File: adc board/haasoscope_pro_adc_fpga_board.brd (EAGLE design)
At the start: 224.5 x 160 mm, 635 parts, among them CN2 12Vin, IC1 ADC12DL2500ACF, IC10 TPS72325DBVR, IC13 LMH5401IRMST, IC14 LMH6401IRMZR, IC15 SN74AVC4T774PWR, IC17 DAC8562SDGSR, IC18 TLV9102IPWR, IC2 SN74AVC4T774PWR, IC21 LMH5401IRMST, IC22 TPS7A7200RGTR, IC23 TPS7A7200RGTR, IC24 TPS7A7200RGTR, IC25 TPS72325DBVR, IC26 TPS7A7200RGTR, IC27 TPS7A7200RGTR, IC28 TPS7A7200RGTR, IC29 LMH6401IRMZR, IC3 ADC122S021CIMM_NOPB, IC30 SN74AVC4T774PWR, IC33 TLV9102IPWR, IC4 TLV9102IPWR, IC5 EP4CE30F23C6N, IC6 EPCQ16ASI8N, IC7 TPS7A7200RGTR, IC8 FT232HQ, IC9 93LC56B, J1 2p-2.54, J11 8pin, J15 test1, J2 test1, J3 2p-2.54, J30 2p-2.54, J31 2p-2.54, J32 2p-2.54, J33 2p-2.54, J34 2p-2.54, J35 2p-2.54, J36 2p-2.54, J37 2p-2.54, J39 2p-2.54, J4 2p-2.54, J40 2p-2.54, J41 2p-2.54, J42 2p-2.54, J43 2p-2.54, J44 2p-2.54, J45 2p-2.54, J46 2p-2.54, J5 1x4, K1 G6K-2F-RF-T-TR03_DC5, K2 G6K-2F-RF-T-TR03_DC5, K3 G6K-2F-RF-T-TR03_DC5, K4 G6K-2F-RF-T-TR03_DC5, K5 G6K-2F-RF-T-TR03_DC5, K6 TLP3475_TP,F, K7 TLP3475_TP,F, Q1 S8050, Q2 FDN340P, Q4 S8050, Q5 S8050, Q7 S8050, Q8 S8050, Q9 S8050, SW3 SKQGADE010, SW4 SKQGADE010, U2 ADF4350BCPZ, X1 USBC, Y2 OSCILLATORSMD-5X3, Y3 12MHz

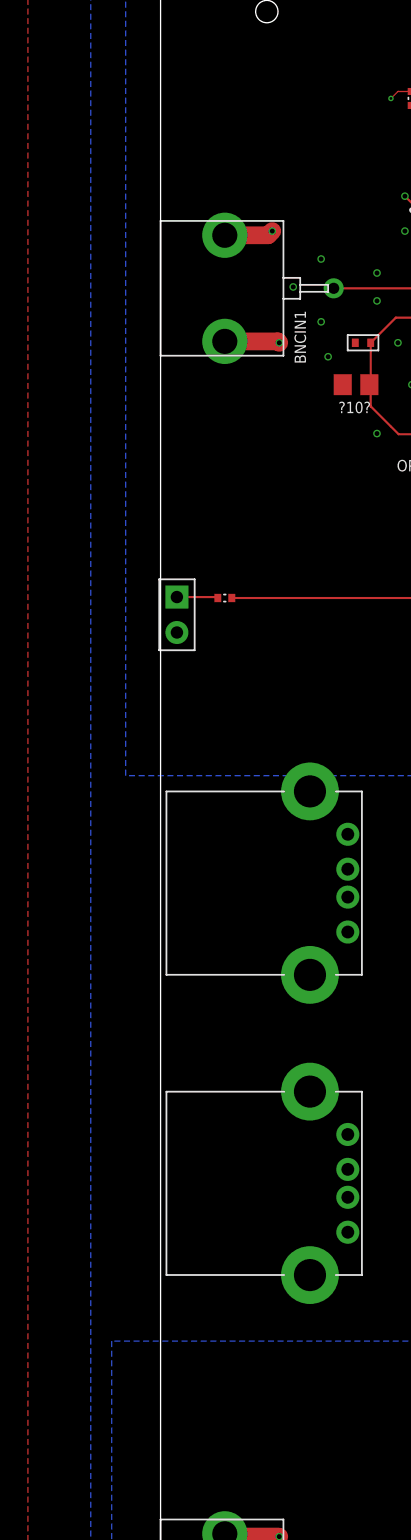
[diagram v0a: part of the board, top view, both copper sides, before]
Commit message: add light pipes for front leds
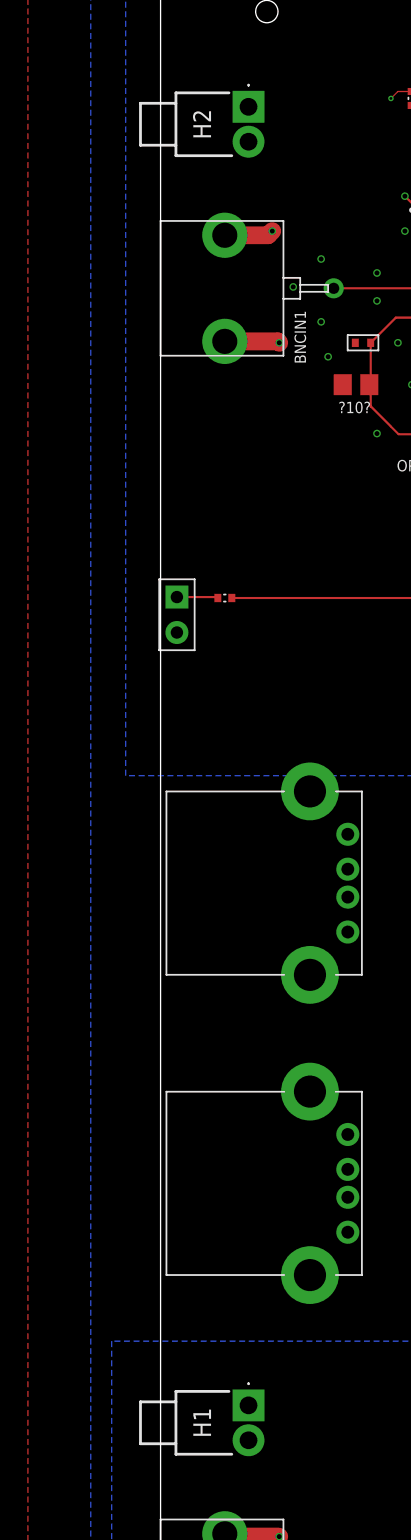
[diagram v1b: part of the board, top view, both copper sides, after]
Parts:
- added H1, H2: SLP3-150-100-F, SLP3-150-100-F:SLP3150100F
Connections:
- net GND: now also H1.1, H1.2, H2.1, H2.2
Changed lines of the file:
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@@
 <setting verticaltext="up"/>
 </settings>
-<grid distance="1" unitdist="mm" unit="mm" style="lines" multiple="1" display="no" altdistance="0.01" altunitdist="mm" altunit="mm"/>
+<grid distance="1" unitdist="mm" unit="mm" style="lines" multiple="1" display="yes" altdistance="0.01" altunitdist="mm" altunit="mm"/>
 <layers>
 <layer number="1" name="top" color="12" fill="1" visible="yes" active="yes"/>
@@
 <element name="R167" library="FlashPCB_Resistors" package="RES-0402" value="10k" x="203" y="94" smashed="yes"/>
 <element name="R246" library="FlashPCB_Resistors" package="RES-0402" value="10k" x="203.01" y="95.41" smashed="yes"/>
+<element name="H1" library="SLP3-150-100-F" package="SLP3150100F" value="SLP3-150-100-F" x="6.3" y="53.4" smashed="yes" rot="R270">
+<attribute name="DESCRIPTION" value="LED Light Pipes Light Pipe Rigid 3mm Right Angle" x="6.3" y="53.4" size="0.8128" layer="27" rot="R270" display="off"/>
+<attribute name="HEIGHT" value="5.4mm" x="6.3" y="53.4" size="0.8128" layer="27" rot="R270" display="off"/>
+<attribute name="MANUFACTURER_NAME" value="Bivar" x="6.3" y="53.4" size="0.8128" layer="27" rot="R270" display="off"/>
+<attribute name="MANUFACTURER_PART_NUMBER" value="SLP3-150-100-F" x="6.3" y="53.4" size="0.8128" layer="27" rot="R270" display="off"/>
+<attribute name="MOUSER_PART_NUMBER" value="749-SLP3-150-100-F" x="6.3" y="53.4" size="0.8128" layer="27" rot="R270" display="off"/>
+<attribute name="MOUSER_PRICE-STOCK" value="https://www.mouser.co.uk/ProductDetail/Bivar/SLP3-150-100-F?qs=6qR8IwHvvod8lAECqeEkXA%3D%3D" x="6.3" y="53.4" size="0.8128" layer="27" rot="R270" display="off"/>
+<attribute name="NAME" x="2.98" y="52.15" size="1.27" layer="25" rot="R270" align="center"/>
+</element>
+<element name="H2" library="SLP3-150-100-F" package="SLP3150100F" value="SLP3-150-100-F" x="6.3" y="146.4" smashed="yes" rot="R270">
+<attribute name="DESCRIPTION" value="LED Light Pipes Light Pipe Rigid 3mm Right Angle" x="6.3" y="146.4" size="0.8128" layer="27" rot="R270" display="off"/>
+<attribute name="HEIGHT" value="5.4mm" x="6.3" y="146.4" size="0.8128" layer="27" rot="R270" display="off"/>
+<attribute name="MANUFACTURER_NAME" value="Bivar" x="6.3" y="146.4" size="0.8128" layer="27" rot="R270" display="off"/>
+<attribute name="MANUFACTURER_PART_NUMBER" value="SLP3-150-100-F" x="6.3" y="146.4" size="0.8128" layer="27" rot="R270" display="off"/>
+<attribute name="MOUSER_PART_NUMBER" value="749-SLP3-150-100-F" x="6.3" y="146.4" size="0.8128" layer="27" rot="R270" display="off"/>
+<attribute name="MOUSER_PRICE-STOCK" value="https://www.mouser.co.uk/ProductDetail/Bivar/SLP3-150-100-F?qs=6qR8IwHvvod8lAECqeEkXA%3D%3D" x="6.3" y="146.4" size="0.8128" layer="27" rot="R270" display="off"/>
+<attribute name="NAME" x="2.98" y="145.15" size="1.27" layer="25" rot="R270" align="center"/>
+</element>
 </elements>
 <signals>
@@
 <via x="199.99" y="92" extent="1-16" drill="0.35"/>
 <wire x1="199.99" y1="90.96" x2="199.99" y2="92" width="0.254" layer="1"/>
+<contactref element="H1" pad="2"/>
+<contactref element="H2" pad="2"/>
+<contactref element="H1" pad="1"/>
+<contactref element="H2" pad="1"/>
 </signal>
 <signal name="3V3" class="1">

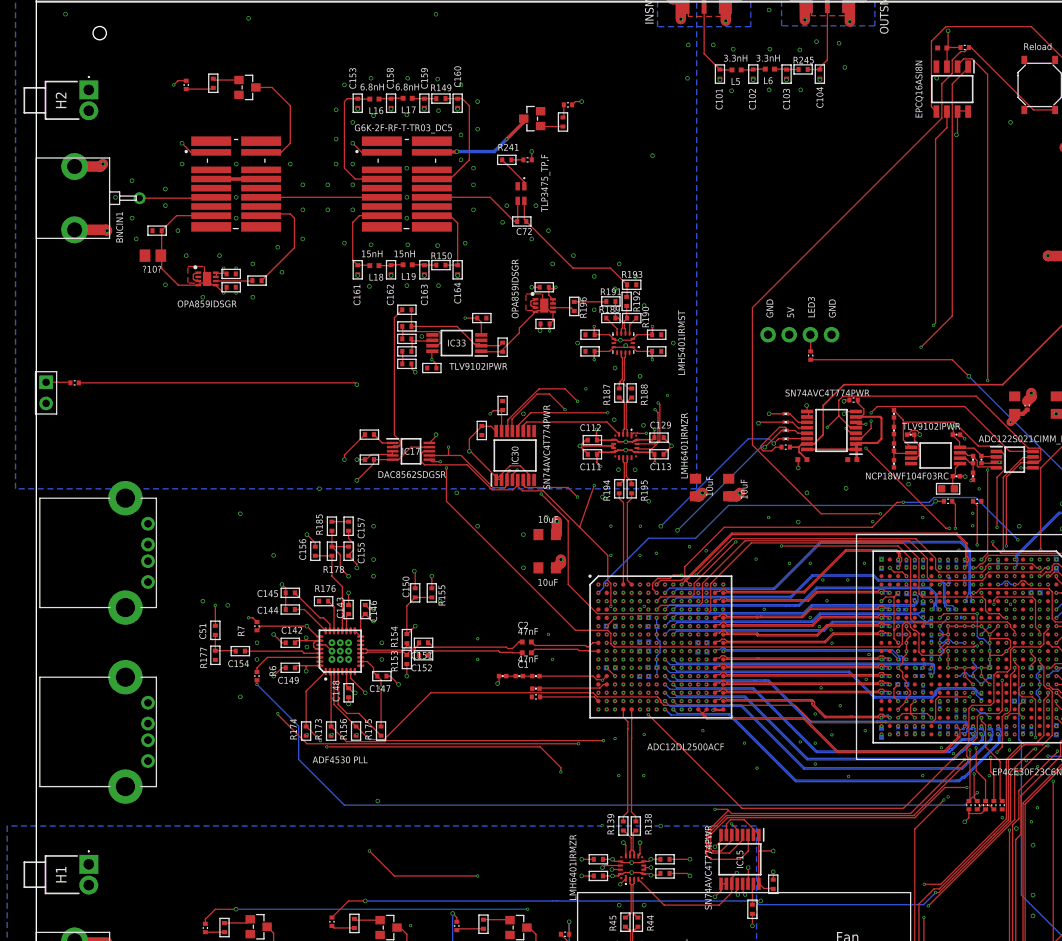
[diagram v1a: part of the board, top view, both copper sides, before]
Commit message: add leds on main board under light pipes
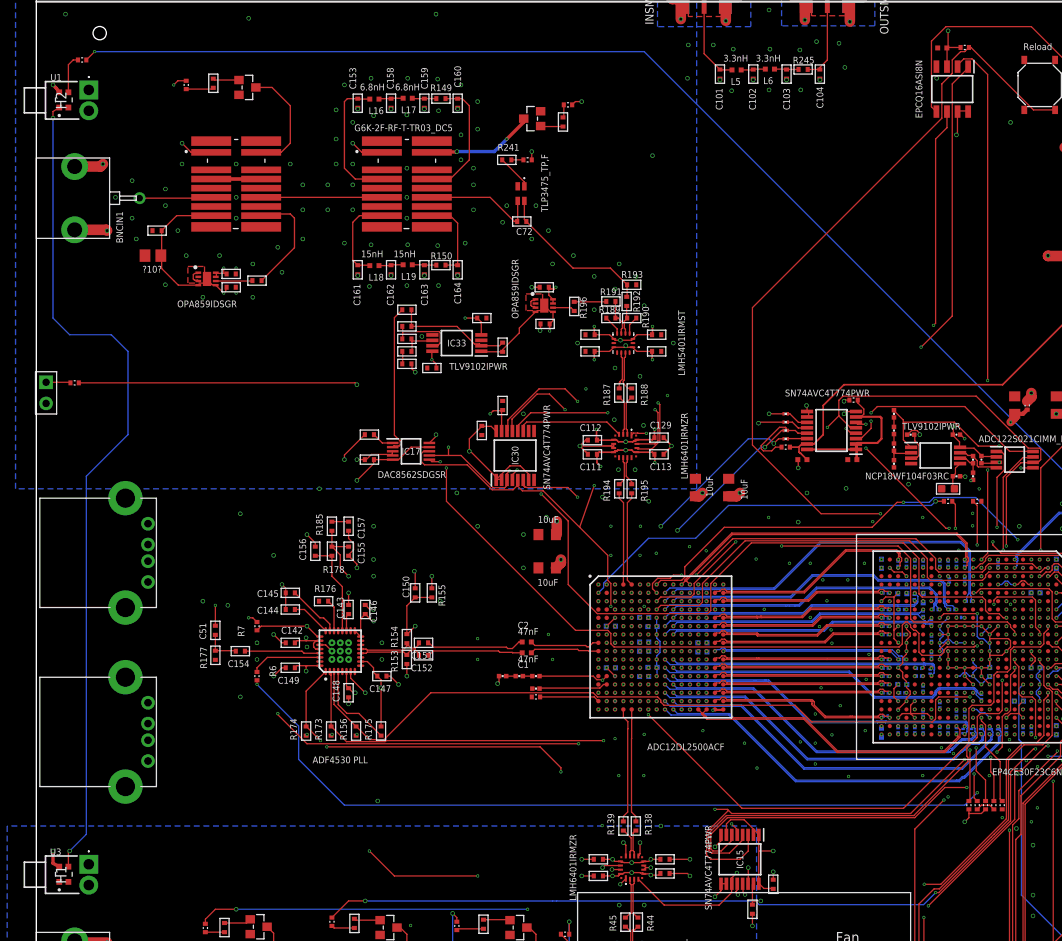
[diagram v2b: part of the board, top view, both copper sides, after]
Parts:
- removed J5: 1x4, SparkFun-Connectors:1X04_NO_SILK
- added U1, U3: WS2812-2020, WS2812-2020:LED_WS2812-2020
- moved R50 94.4 mm to (5.50, 150.0), turned to 180 degrees
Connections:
- new net N$85: U1.1, U3.3
- net 5V: now also U1.4, U3.4; no longer J5.3
- net GND: now also U1.2, U3.2; no longer J5.1, J5.4
- net N$44: now also U1.3; no longer J5.2
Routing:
- net LED3: track 54.9 -> 157.7 mm
- net N$85: track 0.00 -> 101.2 mm, vias 0 -> 2
- net 5V: track 84.5 -> 88.0 mm, vias 20 -> 22
- net N$44: track 2.02 -> 4.70 mm
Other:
- board text removed: "LED3"
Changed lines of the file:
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@@
 <text x="123.5" y="14.5" size="0.8128" layer="21" rot="R90">LED1</text>
 <text x="129.66" y="93.12" size="0.8128" layer="21">LED2</text>
-<text x="93.5" y="119" size="0.8128" layer="21" rot="R90">LED3</text>
 <text x="120.5" y="9" size="0.8128" layer="21" rot="R90">D0</text>
 <text x="123.5" y="9" size="0.8128" layer="21" rot="R90">D1</text>
@@
 <text x="94" y="20" size="0.8128" layer="21" rot="R270">Bin1</text>
 <text x="96.5" y="20" size="0.8128" layer="21" rot="R270">Bin0</text>
-<text x="96" y="119" size="0.8128" layer="21" rot="R90">GND</text>
-<text x="91" y="119" size="0.8128" layer="21" rot="R90">5V</text>
-<text x="88.5" y="119" size="0.8128" layer="21" rot="R90">GND</text>
 <circle x="156" y="74.83" radius="0.2" width="0.508" layer="21"/>
 <text x="182" y="90" size="1.778" layer="21">+</text>
@@
 <element name="R48" library="FlashPCB_Resistors" package="RES-0402" value="1k" x="122" y="12.5" smashed="yes" rot="R270"/>
 <element name="R49" library="FlashPCB_Resistors" package="RES-0402" value="1k" x="119" y="12.5" smashed="yes" rot="R270"/>
-<element name="R50" library="FlashPCB_Resistors" package="RES-0402" value="357" x="93" y="114.5" smashed="yes" rot="R90"/>
+<element name="R50" library="FlashPCB_Resistors" package="RES-0402" value="357" x="5.5" y="150" smashed="yes" rot="R180"/>
 <element name="R51" library="FlashPCB_Resistors" package="RES-0402" value="1k" x="128.5" y="92.5" smashed="yes"/>
 <element name="R52" library="FlashPCB_Resistors" package="RES-0402" value="1k" x="122" y="18" smashed="yes" rot="R270"/>
@@
 <attribute name="WATTAGE" value="" x="48.59" y="125.36" size="1.778" layer="27" rot="R180" display="off"/>
 </element>
-<element name="J5" library="SparkFun-Connectors" library_urn="urn:adsk.eagle:library:513" package="1X04_NO_SILK" package3d_urn="urn:adsk.eagle:package:38094/1" value="1x4" x="95.5" y="117" smashed="yes" rot="R180">
-<attribute name="PROD_ID" value="CONN-09696" x="95.5" y="117" size="1.778" layer="27" rot="R180" display="off"/>
-</element>
 <element name="C81" library="Nordic_nRF" library_urn="urn:adsk.eagle:library:169009" package="RESC0805_N" package3d_urn="urn:adsk.eagle:package:2593736/1" value="22uF" x="188" y="91.5" smashed="yes">
 <attribute name="VALUE" x="186.5" y="92.95" size="0.8128" layer="21"/>
@@
 <attribute name="NAME" x="2.98" y="145.15" size="1.27" layer="25" rot="R270" align="center"/>
 </element>
+<element name="U1" library="WS2812-2020" package="LED_WS2812-2020" value="WS2812-2020" x="3.3" y="145.2" smashed="yes" rot="R270">
+<attribute name="AVAILABILITY" value="Not in stock" x="3.3" y="145.2" size="0.8128" layer="27" rot="R270" display="off"/>
+<attribute name="CHECK_PRICES" value="https://www.snapeda.com/parts/WS2812-2020/Worldsemi/view-part/?ref=eda" x="3.3" y="145.2" size="0.8128" layer="27" rot="R270" display="off"/>
+<attribute name="DESCRIPTION" value="                                                      Intelligent control LED light source, SMD-4                                              " x="3.3" y="145.2" size="0.8128" layer="27" rot="R270" display="off"/>
+<attribute name="MF" value="Worldsemi" x="3.3" y="145.2" size="0.8128" layer="27" rot="R270" display="off"/>
+<attribute name="MP" value="WS2812-2020" x="3.3" y="145.2" size="0.8128" layer="27" rot="R270" display="off"/>
+<attribute name="NAME" x="1.675" y="147.48606875" size="0.8128" layer="25"/>
+<attribute name="PACKAGE" value="Package " x="3.3" y="145.2" size="0.8128" layer="27" rot="R270" display="off"/>
+<attribute name="PRICE" value="None" x="3.3" y="145.2" size="0.8128" layer="27" rot="R270" display="off"/>
+<attribute name="SNAPEDA_LINK" value="https://www.snapeda.com/parts/WS2812-2020/Worldsemi/view-part/?ref=snap" x="3.3" y="145.2" size="0.8128" layer="27" rot="R270" display="off"/>
+<attribute name="VALUE" x="1.675" y="142.55336875" size="0.8128" layer="27" align="top-left"/>
+</element>
+<element name="U3" library="WS2812-2020" package="LED_WS2812-2020" value="WS2812-2020" x="3.3" y="52.2" smashed="yes" rot="R270">
+<attribute name="AVAILABILITY" value="Not in stock" x="3.3" y="52.2" size="0.8128" layer="27" rot="R270" display="off"/>
+<attribute name="CHECK_PRICES" value="https://www.snapeda.com/parts/WS2812-2020/Worldsemi/view-part/?ref=eda" x="3.3" y="52.2" size="0.8128" layer="27" rot="R270" display="off"/>
+<attribute name="DESCRIPTION" value="                                                      Intelligent control LED light source, SMD-4                                              " x="3.3" y="52.2" size="0.8128" layer="27" rot="R270" display="off"/>
+<attribute name="MF" value="Worldsemi" x="3.3" y="52.2" size="0.8128" layer="27" rot="R270" display="off"/>
+<attribute name="MP" value="WS2812-2020" x="3.3" y="52.2" size="0.8128" layer="27" rot="R270" display="off"/>
+<attribute name="NAME" x="1.635" y="54.48606875" size="0.8128" layer="25"/>
+<attribute name="PACKAGE" value="Package " x="3.3" y="52.2" size="0.8128" layer="27" rot="R270" display="off"/>
+<attribute name="PRICE" value="None" x="3.3" y="52.2" size="0.8128" layer="27" rot="R270" display="off"/>
+<attribute name="SNAPEDA_LINK" value="https://www.snapeda.com/parts/WS2812-2020/Worldsemi/view-part/?ref=snap" x="3.3" y="52.2" size="0.8128" layer="27" rot="R270" display="off"/>
+<attribute name="VALUE" x="1.635" y="49.55336875" size="0.8128" layer="27" align="top-left"/>
+</element>
 </elements>
 <signals>
@@
 <via x="99.55" y="69.45" extent="1-16" drill="0.2"/>
 <contactref element="LED43" pad="C"/>
-<contactref element="J5" pad="1"/>
-<contactref element="J5" pad="4"/>
 <wire x1="190.8" y1="83.3" x2="189.2" y2="83.3" width="1.27" layer="1"/>
 <contactref element="J45" pad="2"/>
@@
 <contactref element="H1" pad="1"/>
 <contactref element="H2" pad="1"/>
+<contactref element="U1" pad="2"/>
+<contactref element="U3" pad="2"/>
 </signal>
 <signal name="3V3" class="1">
@@
 <contactref element="IC5" pad="A8"/>
 <contactref element="R50" pad="P$1"/>
-<wire x1="93" y1="114" x2="110" y2="114" width="0.0889" layer="1"/>
-<wire x1="110" y1="114" x2="112" y2="112" width="0.0889" layer="1"/>
-<via x="112" y="112" extent="1-16" drill="0.35"/>
-<wire x1="112" y1="112" x2="117.12855" y2="106.87145" width="0.0889" layer="16"/>
-<wire x1="117.12855" y1="106.87145" x2="117.1538625" y2="106.87145" width="0.0889" layer="16"/>
+<wire x1="117.1538625" y1="106.87145" x2="117.12855" y2="106.87145" width="0.0889" layer="16"/>
 <wire x1="117.1538625" y1="106.87145" x2="124.5" y2="99.5253125" width="0.0889" layer="16"/>
 <via x="124.5" y="98.5" extent="1-16" drill="0.35"/>
@@
 <wire x1="122.52725625" y1="82.97274375" x2="122.5" y2="83" width="0.0889" layer="1"/>
 <wire x1="124.5" y1="99.5253125" x2="124.5" y2="98.5" width="0.0889" layer="16"/>
+<via x="7" y="151" extent="1-16" drill="0.2"/>
+<wire x1="7" y1="151" x2="6" y2="150" width="0.0889" layer="1"/>
+<wire x1="117.12855" y1="106.87145" x2="73" y2="151" width="0.0889" layer="16"/>
+<wire x1="73" y1="151" x2="7" y2="151" width="0.0889" layer="16"/>
 </signal>
 <signal name="CLKEXT" class="5">
@@
 <wire x1="16" y1="41" x2="17.1" y2="39.9" width="0.16" layer="1"/>
 <wire x1="17.1" y1="39.9" x2="19.5" y2="39.9" width="0.16" layer="1"/>
-<contactref element="J5" pad="3"/>
 <wire x1="147" y1="72" x2="147.4045" y2="71.5955" width="0.25" layer="1"/>
 <wire x1="147.4045" y1="71.5955" x2="147.4045" y2="70.917" width="0.25" layer="1"/>
@@
 <wire x1="161.1" y1="88" x2="160.1" y2="87" width="2.54" layer="1"/>
 <wire x1="160.1" y1="87" x2="160" y2="87" width="2.54" layer="1"/>
+<contactref element="U3" pad="4"/>
+<contactref element="U1" pad="4"/>
+<via x="2" y="147" extent="1-16" drill="0.35"/>
+<wire x1="2" y1="147" x2="2.42" y2="146.58" width="0.4064" layer="1"/>
+<wire x1="2.42" y1="146.58" x2="2.75" y2="146.115" width="0.4064" layer="1"/>
+<via x="2" y="55" extent="1-16" drill="0.35"/>
+<wire x1="2.75" y1="53.115" x2="2" y2="53.515" width="0.4064" layer="1"/>
+<wire x1="2" y1="53.515" x2="2" y2="55" width="0.4064" layer="1"/>
 </signal>
 <signal name="COIL1-">
@@
 <wire x1="46.61" y1="125.36" x2="48.04" y2="125.36" width="0.16" layer="1"/>
 </signal>
-<signal name="N$44">
-<contactref element="J5" pad="2"/>
-<contactref element="R50" pad="P$2"/>
-<wire x1="92.96" y1="117" x2="93" y2="116.96" width="0.0889" layer="1"/>
-<wire x1="93" y1="116.96" x2="93" y2="115" width="0.0889" layer="1"/>
-</signal>
 <signal name="5VDIRTY" class="1">
 <contactref element="R237" pad="P$2"/>
@@
 <wire x1="203.51" y1="95.41" x2="204.6" y2="95.41" width="0.254" layer="1"/>
 </signal>
+<signal name="N$44">
+<contactref element="U1" pad="3"/>
+<contactref element="R50" pad="P$2"/>
+<wire x1="3.85" y1="146.115" x2="3.85" y2="149.428065625" width="0.0889" layer="1"/>
+<wire x1="3.85" y1="149.428065625" x2="4.421934375" y2="150" width="0.0889" layer="1"/>
+<wire x1="4.421934375" y1="150" x2="5" y2="150" width="0.0889" layer="1"/>
+</signal>
+<signal name="N$85">
+<contactref element="U1" pad="1"/>
+<contactref element="U3" pad="3"/>
+<wire x1="2.75" y1="144.285" x2="2" y2="143.805" width="0.127" layer="1"/>
+<wire x1="2" y1="143.805" x2="2" y2="143" width="0.127" layer="1"/>
+<via x="2" y="143" extent="1-16" drill="0.35"/>
+<wire x1="2" y1="143" x2="2" y2="119" width="0.127" layer="16"/>
+<wire x1="2" y1="119" x2="4" y2="117" width="0.127" layer="16"/>
+<wire x1="4" y1="117" x2="9" y2="117" width="0.127" layer="16"/>
+<wire x1="9" y1="117" x2="11" y2="115" width="0.127" layer="16"/>
+<wire x1="11" y1="115" x2="11" y2="105" width="0.127" layer="16"/>
+<wire x1="11" y1="105" x2="6" y2="100" width="0.127" layer="16"/>
+<wire x1="6" y1="100" x2="6" y2="57" width="0.127" layer="16"/>
+<wire x1="4" y1="55" x2="6" y2="57" width="0.127" layer="16"/>
+<via x="4" y="55" extent="1-16" drill="0.35"/>
+<wire x1="3.85" y1="53.115" x2="3.85" y2="54.85" width="0.0889" layer="1"/>
+<wire x1="3.85" y1="54.85" x2="4" y2="55" width="0.0889" layer="1"/>
+</signal>
 </signals>
